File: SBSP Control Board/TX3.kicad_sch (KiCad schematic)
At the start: 13 parts, among them U4 ADAR1000ACCZN

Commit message: first rev of trans. line routed
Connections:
- net TX3 renamed TX4
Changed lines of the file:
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@@
 		)
 	)
-	(global_label "TX3"
+	(global_label "TX4"
 		(shape input)
 		(at 149.86 132.08 180)

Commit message: 'finished' the first IC routing
need to re do and see what connections we need to make for programming. also need to see about better ground connections to the IC.
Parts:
- C31, C32, C33, C34, C35, C36, C37, C38, C53, C54, C55: footprint Capacitor_SMD:C_1206_3216Metric -> Resistor_SMD:R_0603_1608Metric
- R14: footprint Resistor_SMD:R_1206_3216Metric -> Resistor_SMD:R_0603_1608Metric
- U4: footprint CC-88-1_ADI -> adar1000:CC-88-1_ADI
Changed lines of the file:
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@@
 			)
 		)
-		(property "Footprint" "Resistor_SMD:R_1206_3216Metric"
+		(property "Footprint" "Resistor_SMD:R_0603_1608Metric"
 			(at 140.97 103.378 90)
 			(hide yes)
@@
 			)
 		)
-		(property "Footprint" "Capacitor_SMD:C_1206_3216Metric"
+		(property "Footprint" "Resistor_SMD:R_0603_1608Metric"
 			(at 167.3352 193.04 0)
 			(hide yes)
@@
 			)
 		)
-		(property "Footprint" "CC-88-1_ADI"
+		(property "Footprint" "adar1000:CC-88-1_ADI"
 			(at 158.75 153.67 0)
 			(hide yes)
@@
 			)
 		)
-		(property "Footprint" "Capacitor_SMD:C_1206_3216Metric"
+		(property "Footprint" "Resistor_SMD:R_0603_1608Metric"
 			(at 180.0352 193.04 0)
 			(hide yes)
@@
 			)
 		)
-		(property "Footprint" "CC-88-1_ADI"
+		(property "Footprint" "adar1000:CC-88-1_ADI"
 			(at 171.45 252.73 0)
 			(hide yes)
@@
 			)
 		)
-		(property "Footprint" "Capacitor_SMD:C_1206_3216Metric"
+		(property "Footprint" "Resistor_SMD:R_0603_1608Metric"
 			(at 192.7352 193.04 0)
 			(hide yes)
@@
 			)
 		)
-		(property "Footprint" "CC-88-1_ADI"
+		(property "Footprint" "adar1000:CC-88-1_ADI"
 			(at 149.86 71.12 0)
 			(hide yes)
@@
 			)
 		)
-		(property "Footprint" "Capacitor_SMD:C_1206_3216Metric"
+		(property "Footprint" "Resistor_SMD:R_0603_1608Metric"
 			(at 112.7252 166.37 0)
 			(hide yes)
@@
 			)
 		)
-		(property "Footprint" "Capacitor_SMD:C_1206_3216Metric"
+		(property "Footprint" "Resistor_SMD:R_0603_1608Metric"
 			(at 219.4052 193.04 0)
 			(hide yes)
@@
 			)
 		)
-		(property "Footprint" "Capacitor_SMD:C_1206_3216Metric"
+		(property "Footprint" "Resistor_SMD:R_0603_1608Metric"
 			(at 206.7052 193.04 0)
 			(hide yes)
@@
 			)
 		)
-		(property "Footprint" "Capacitor_SMD:C_1206_3216Metric"
+		(property "Footprint" "Resistor_SMD:R_0603_1608Metric"
 			(at 124.1552 166.37 0)
 			(hide yes)
@@
 			)
 		)
-		(property "Footprint" "Capacitor_SMD:C_1206_3216Metric"
+		(property "Footprint" "Resistor_SMD:R_0603_1608Metric"
 			(at 101.2952 166.37 0)
 			(hide yes)
@@
 			)
 		)
-		(property "Footprint" "Capacitor_SMD:C_1206_3216Metric"
+		(property "Footprint" "Resistor_SMD:R_0603_1608Metric"
 			(at 140.6652 193.04 0)
 			(hide yes)
@@
 			)
 		)
-		(property "Footprint" "Capacitor_SMD:C_1206_3216Metric"
+		(property "Footprint" "Resistor_SMD:R_0603_1608Metric"
 			(at 127.9652 193.04 0)
 			(hide yes)
@@
 			)
 		)
-		(property "Footprint" "Capacitor_SMD:C_1206_3216Metric"
+		(property "Footprint" "Resistor_SMD:R_0603_1608Metric"
 			(at 154.6352 193.04 0)
 			(hide yes)

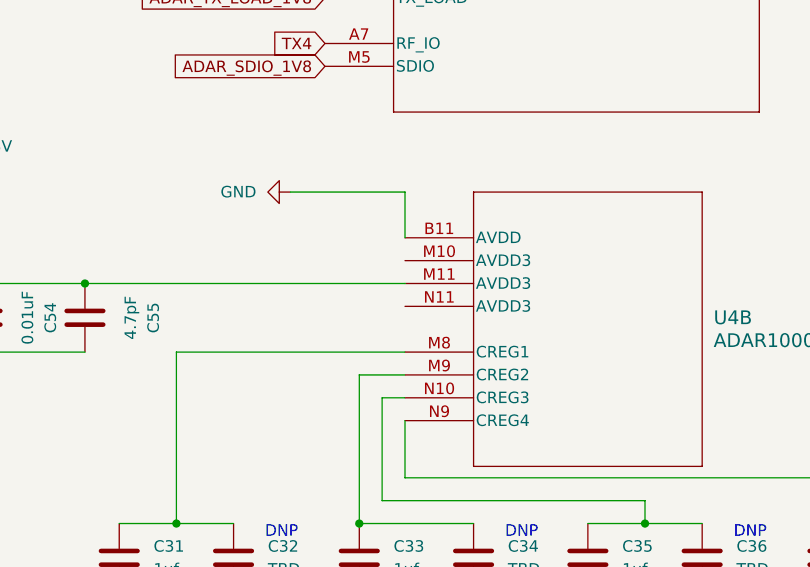
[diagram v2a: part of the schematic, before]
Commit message: finished passive layout for IC's
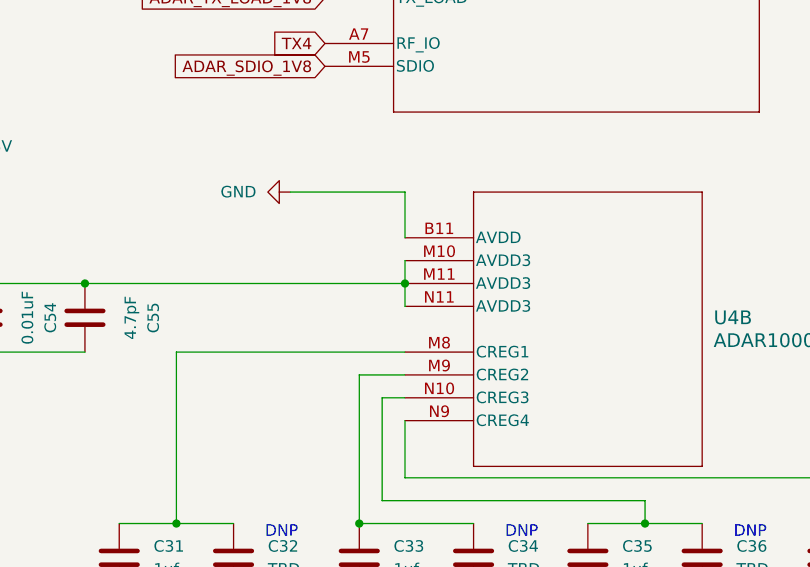
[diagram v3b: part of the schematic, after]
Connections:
- net +3.3V: now also U4.M10 (AVDD3), U4.N11 (AVDD3)
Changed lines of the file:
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@@
 	)
 	(junction
+		(at 158.75 158.75)
+		(diameter 0)
+		(color 0 0 0 0)
+	)
+	(junction
 		(at 153.67 185.42)
 		(diameter 0)
@@
 	(wire
 		(pts
+			(xy 158.75 158.75) (xy 158.75 161.29)
+		)
+		(stroke
+			(width 0)
+			(type default)
+		)
+	)
+	(wire
+		(pts
 			(xy 270.51 252.73) (xy 273.05 252.73)
 		)
@@
 	(wire
 		(pts
+			(xy 158.75 156.21) (xy 158.75 158.75)
+		)
+		(stroke
+			(width 0)
+			(type default)
+		)
+	)
+	(wire
+		(pts
 			(xy 237.49 252.73) (xy 240.03 252.73)
 		)
@@
 		(exclude_from_sim no)
 		(in_bom yes)
-		(on_board yes)
+		(on_board no)
 		(in_pos_files yes)
 		(dnp no)
@@
 		(exclude_from_sim no)
 		(in_bom yes)
-		(on_board yes)
+		(on_board no)
 		(in_pos_files yes)
 		(dnp no)
@@
 		(exclude_from_sim no)
 		(in_bom yes)
-		(on_board yes)
+		(on_board no)
 		(in_pos_files yes)
 		(dnp no)
@@
 		(exclude_from_sim no)
 		(in_bom yes)
-		(on_board yes)
+		(on_board no)
 		(in_pos_files yes)
 		(dnp no)
